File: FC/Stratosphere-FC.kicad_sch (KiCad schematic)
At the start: 53 parts, among them J1 Connector, J2 Conn_01x04, J3 Conn_01x04, J4 Conn_01x04, J5 Conn_01x04, J6 Conn_01x05, J7 Conn_01x04, P2 USB_C_Plug_USB2.0, U1 ICM-42605, U2 W25Q16JVSS, U3 BMP388, U5 AMS1117, U7 915MHz, U8 STM32F405RGTx, X2 Shenzhen SCTF Elec SX2B12.000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

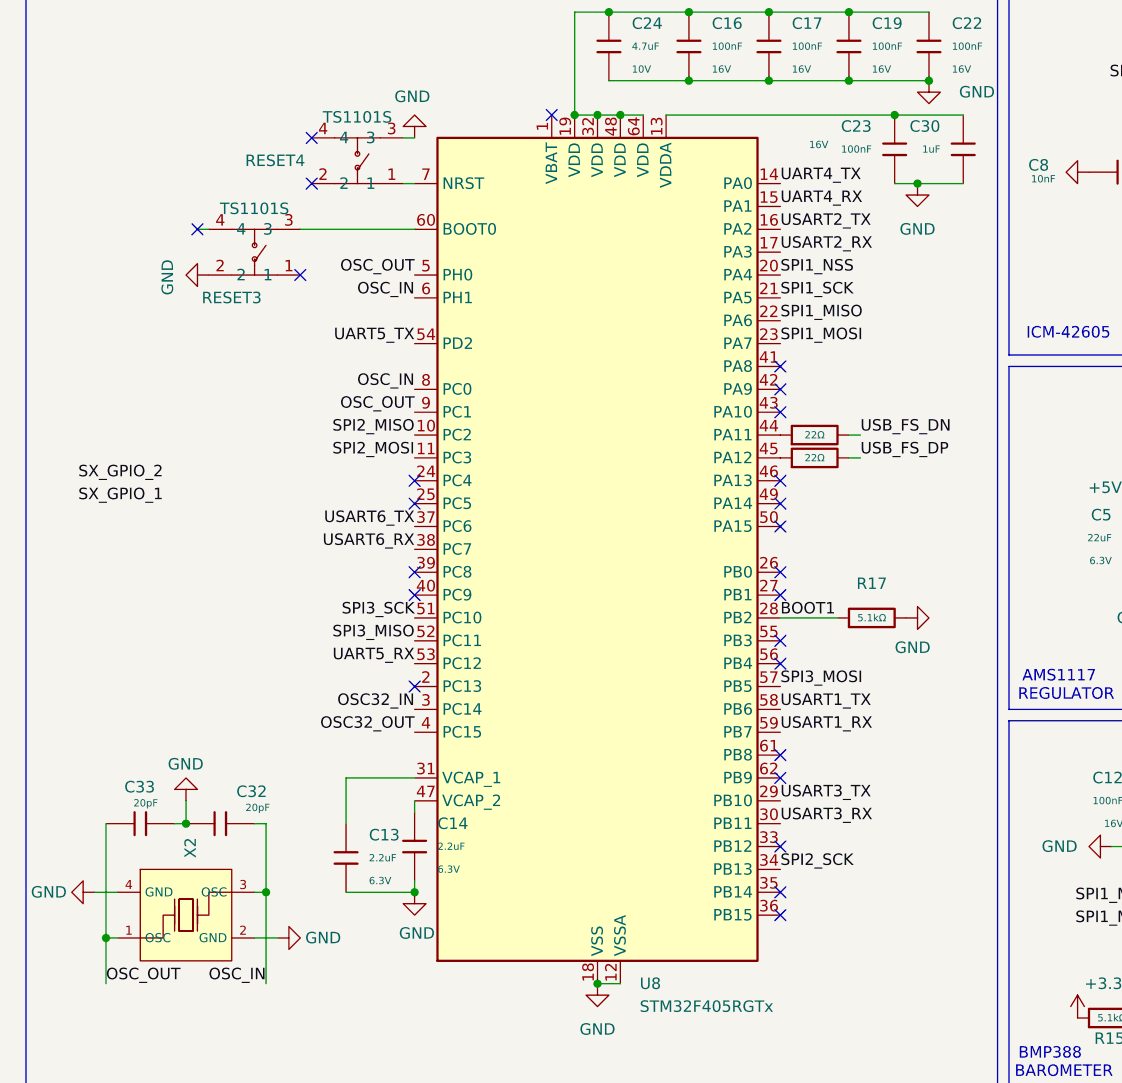
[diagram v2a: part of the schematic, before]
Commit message: Completed pin mapping of STM32
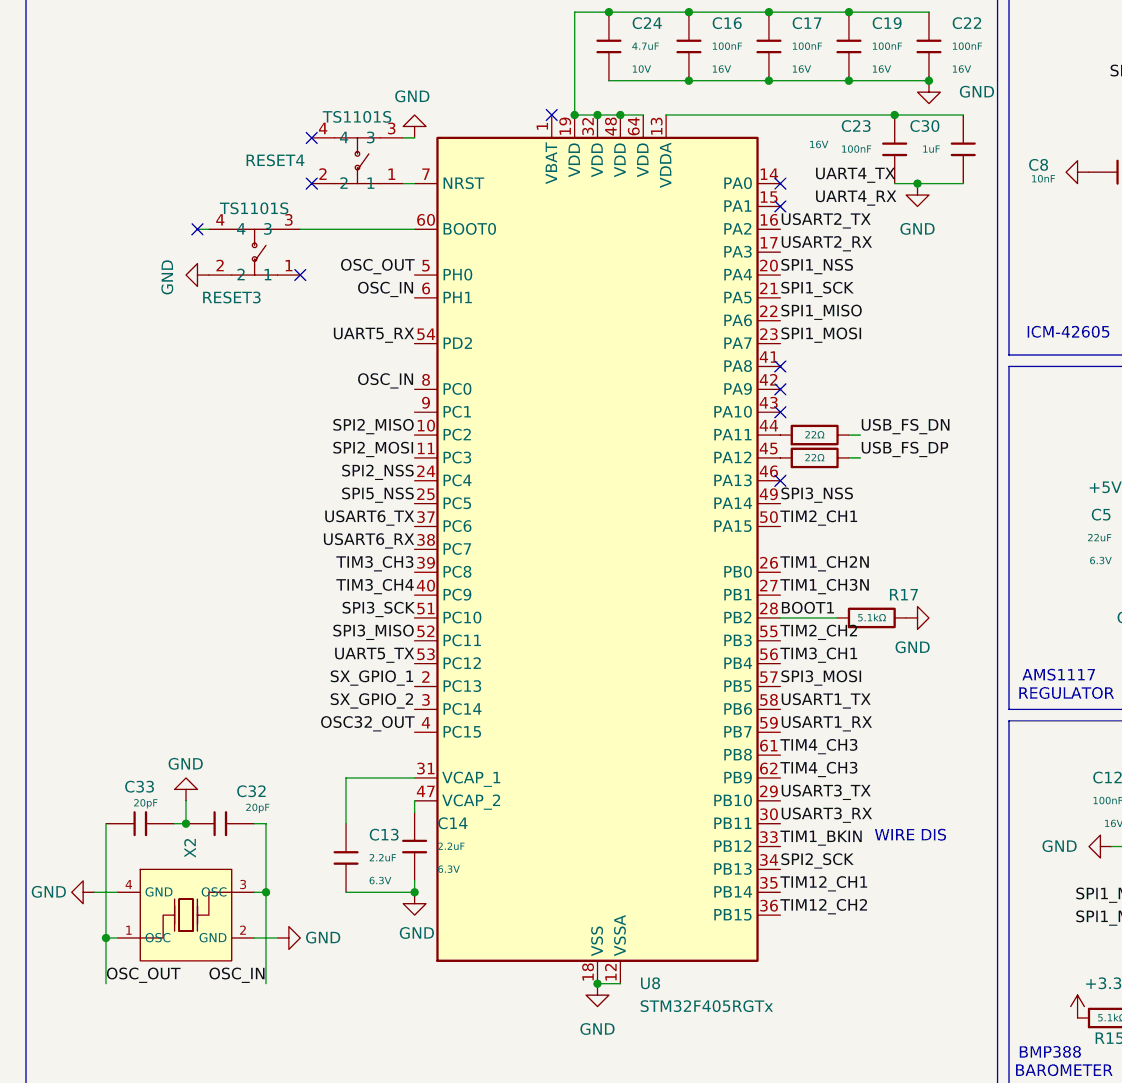
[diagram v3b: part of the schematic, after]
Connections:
- net OSC32_IN is gone; now on net SX_GPIO_2: U8.3 (PC14)
- net OSC_OUT: no longer U8.9 (PC1)
- net SPI2_NSS: now also U8.24 (PC4)
- net SPI3_NSS: now also U8.49 (PA14)
- net SPI5_NSS: now also U8.25 (PC5)
- net SX_GPIO_1: now also U8.2 (PC13)
- net UART4_RX: no longer U8.15 (PA1)
- net UART4_TX: no longer U8.14 (PA0)
- net UART5_RX: now also U8.54 (PD2); no longer U8.53 (PC12)
- net UART5_TX: now also U8.53 (PC12); no longer U8.54 (PD2)
- net TIM1_CH2N: now reaches U8.26 (PB0)
- net TIM1_CH3N: now reaches U8.27 (PB1)
- net TIM1_BKIN: now reaches U8.33 (PB12)
- net TIM12_CH1: now reaches U8.35 (PB14)
- net TIM12_CH2: now reaches U8.36 (PB15)
- net TIM3_CH3: now reaches U8.39 (PC8)
- net TIM3_CH4: now reaches U8.40 (PC9)
- net TIM2_CH1: now reaches U8.50 (PA15)
- net TIM2_CH2: now reaches U8.55 (PB3)
- net TIM3_CH1: now reaches U8.56 (PB4)
- net TIM4_CH3: now reaches U8.61 (PB8)
- net TIM4_CH3: now also U8.62 (PB9)
- no-connect marks 34 -> 20
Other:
- note added: "WIRE DIS"
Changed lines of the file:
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@@
 		)
 	)
+	(text "WIRE DIS\n"
+		(exclude_from_sim no)
+		(at 112.268 108.204 0)
+		(effects
+			(font
+				(size 1.27 1.27)
+			)
+		)
+	)
 	(text "BAROMETER\n"
 		(exclude_from_sim no)
@@
 	)
 	(no_connect
-		(at 97.79 99.06)
-	)
-	(no_connect
-		(at 97.79 101.6)
-	)
-	(no_connect
-		(at 57.15 68.58)
-	)
-	(no_connect
-		(at 97.79 86.36)
-	)
-	(no_connect
-		(at 97.79 71.12)
-	)
-	(no_connect
-		(at 97.79 109.22)
-	)
-	(no_connect
-		(at 57.15 81.28)
+		(at 97.79 35.56)
 	)
 	(no_connect
@@
 	)
 	(no_connect
-		(at 57.15 78.74)
-	)
-	(no_connect
-		(at 97.79 73.66)
-	)
-	(no_connect
 		(at 72.39 27.94)
 	)
@@
 	)
 	(no_connect
+		(at 97.79 38.1)
+	)
+	(no_connect
 		(at 115.57 158.75)
 	)
@@
 	)
 	(no_connect
-		(at 97.79 81.28)
-	)
-	(no_connect
 		(at 44.45 45.72)
 	)
 	(no_connect
-		(at 57.15 71.12)
-	)
-	(no_connect
 		(at 97.79 58.42)
 	)
 	(no_connect
-		(at 97.79 116.84)
-	)
-	(no_connect
-		(at 97.79 114.3)
-	)
-	(no_connect
 		(at 115.57 166.37)
 	)
@@
 	)
 	(no_connect
-		(at 57.15 91.44)
-	)
-	(no_connect
 		(at 45.72 35.56)
 	)
@@
 	)
 	(no_connect
-		(at 97.79 78.74)
-	)
-	(no_connect
 		(at 90.17 168.91)
 	)
@@
 	)
 	(no_connect
-		(at 97.79 88.9)
-	)
-	(no_connect
 		(at 33.02 40.64)
 	)
@@
 	)
 	(label "SX_GPIO_2"
-		(at 29.21 68.58 180)
+		(at 57.15 93.98 180)
 		(effects
 			(font
@@
 		)
 	)
+	(label "UART4_TX"
+		(at 101.6 35.56 0)
+		(effects
+			(font
+				(size 1.27 1.27)
+			)
+			(justify left bottom)
+		)
+	)
 	(label "SPI1_SCK"
 		(at 247.65 31.75 180)
@@
 		)
 	)
+	(label "TIM12_CH1"
+		(at 97.79 114.3 0)
+		(effects
+			(font
+				(size 1.27 1.27)
+			)
+			(justify left bottom)
+		)
+	)
 	(label "SPI3_NSS"
 		(at 78.74 163.83 0)
@@
 		)
 	)
-	(label "UART5_RX"
+	(label "UART5_TX"
 		(at 57.15 88.9 180)
 		(effects
@@
 		)
 	)
+	(label "TIM3_CH1"
+		(at 97.79 88.9 0)
+		(effects
+			(font
+				(size 1.27 1.27)
+			)
+			(justify left bottom)
+		)
+	)
+	(label "TIM4_CH3"
+		(at 97.79 101.6 0)
+		(effects
+			(font
+				(size 1.27 1.27)
+			)
+			(justify left bottom)
+		)
+	)
 	(label "SPI1_MISO"
 		(at 247.65 36.83 180)
@@
 		)
 	)
+	(label "TIM1_CH2N"
+		(at 97.79 78.74 0)
+		(effects
+			(font
+				(size 1.27 1.27)
+			)
+			(justify left bottom)
+		)
+	)
 	(label "SPI3_MOSI"
 		(at 87.63 158.75 180)
@@
 		)
 	)
+	(label "TIM1_CH3N"
+		(at 97.79 81.28 0)
+		(effects
+			(font
+				(size 1.27 1.27)
+			)
+			(justify left bottom)
+		)
+	)
 	(label "PWM_6"
 		(at 191.77 100.33 180)
@@
 	)
 	(label "SX_GPIO_1"
-		(at 29.21 71.12 180)
+		(at 57.15 91.44 180)
 		(effects
 			(font
@@
 		)
 	)
+	(label "TIM2_CH1"
+		(at 97.79 73.66 0)
+		(effects
+			(font
+				(size 1.27 1.27)
+			)
+			(justify left bottom)
+		)
+	)
 	(label "SPI3_MOSI"
 		(at 97.79 91.44 0)
@@
 		)
 	)
+	(label "UART4_RX"
+		(at 101.6 38.1 0)
+		(effects
+			(font
+				(size 1.27 1.27)
+			)
+			(justify left bottom)
+		)
+	)
 	(label "USB_FS_DN"
 		(at 43.18 160.02 0)
@@
 		)
 	)
-	(label "UART5_TX"
+	(label "UART5_RX"
 		(at 57.15 53.34 180)
 		(effects
@@
 		)
 	)
+	(label "TIM3_CH3"
+		(at 57.15 78.74 180)
+		(effects
+			(font
+				(size 1.27 1.27)
+			)
+			(justify right bottom)
+		)
+	)
+	(label "SPI5_NSS"
+		(at 57.15 71.12 180)
+		(effects
+			(font
+				(size 1.27 1.27)
+			)
+			(justify right bottom)
+		)
+	)
 	(label "SPI3_SCK"
 		(at 191.77 62.23 180)
@@
 		)
 	)
+	(label "SPI2_NSS"
+		(at 57.15 68.58 180)
+		(effects
+			(font
+				(size 1.27 1.27)
+			)
+			(justify right bottom)
+		)
+	)
 	(label "SPI3_MISO"
 		(at 87.63 156.21 180)
@@
 		)
 	)
+	(label "TIM1_BKIN"
+		(at 97.79 109.22 0)
+		(effects
+			(font
+				(size 1.27 1.27)
+			)
+			(justify left bottom)
+		)
+	)
 	(label "OSC_OUT"
 		(at 57.15 45.72 180)
@@
 		)
 	)
+	(label "TIM12_CH2"
+		(at 97.79 116.84 0)
+		(effects
+			(font
+				(size 1.27 1.27)
+			)
+			(justify left bottom)
+		)
+	)
 	(label "SPI1_MOSI"
 		(at 97.79 53.34 0)
@@
 		)
 	)
-	(label "USART2_RX"
-		(at 97.79 43.18 0)
+	(label "SPI2_SCK"
+		(at 97.79 111.76 0)
 		(effects
 			(font
@@
 		)
 	)
-	(label "SPI1_SCK"
-		(at 151.13 102.87 180)
+	(label "TIM4_CH3"
+		(at 97.79 99.06 0)
 		(effects
 			(font
 				(size 1.27 1.27)
 			)
-			(justify right bottom)
+			(justify left bottom)
 		)
 	)
-	(label "UART4_TX"
-		(at 97.79 35.56 0)
+	(label "USART2_RX"
+		(at 97.79 43.18 0)
 		(effects
 			(font
@@
 		)
 	)
-	(label "PWM_1"
-		(at 191.77 82.55 180)
+	(label "SPI1_SCK"
+		(at 151.13 102.87 180)
 		(effects
 			(font
@@
 		)
 	)
-	(label "OSC32_IN"
-		(at 57.15 93.98 180)
+	(label "TIM3_CH4"
+		(at 57.15 81.28 180)
+		(effects
+			(font
+				(size 1.27 1.27)
+			)
+			(justify right bottom)
+		)
+	)
+	(label "PWM_1"
+		(at 191.77 82.55 180)
 		(effects
 			(font
@@
 		)
 	)
-	(label "SPI2_SCK"
-		(at 97.79 111.76 0)
-		(effects
-			(font
-				(size 1.27 1.27)
-			)
-			(justify left bottom)
-		)
-	)
 	(label "SPI3_SCK"
 		(at 87.63 161.29 180)
@@
 		)
 	)
+	(label "SPI3_NSS"
+		(at 97.79 71.12 0)
+		(effects
+			(font
+				(size 1.27 1.27)
+			)
+			(justify left bottom)
+		)
+	)
 	(label "USB_FS_DP"
 		(at 106.68 66.04 0)
@@
 		)
 	)
-	(label "OSC_OUT"
-		(at 57.15 60.96 180)
+	(label "SPI3_MISO"
+		(at 191.77 64.77 180)
 		(effects
 			(font
@@
 	)
 	(label "SPI3_MISO"
-		(at 191.77 64.77 180)
+		(at 57.15 86.36 180)
 		(effects
 			(font
@@
 		)
 	)
-	(label "SPI3_MISO"
-		(at 57.15 86.36 180)
+	(label "TIM2_CH2"
+		(at 97.79 86.36 0)
 		(effects
 			(font
 				(size 1.27 1.27)
 			)
-			(justify right bottom)
+			(justify left bottom)
 		)
 	)
@@
 		)
 	)
-	(label "UART4_RX"
-		(at 97.79 38.1 0)
-		(effects
-			(font
-				(size 1.27 1.27)
-			)
-			(justify left bottom)
-		)
-	)
 	(symbol
 		(lib_id "PCM_JLCPCB-Resistors:0402,200Ω")
@@
 		(on_board yes)
 		(dnp no)
-		(fields_autoplaced yes)
 		(property "Reference" "R17"
-			(at 107.95 80.01 90)
+			(at 111.506 81.28 90)
 			(effects
 				(font
